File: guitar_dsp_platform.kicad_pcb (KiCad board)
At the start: 4 copper layers, 122 x 122 mm, 159 parts, among them J201 NMJ6HCD2, J202 NMJ6HCD2, J203 NMJ6HCD2, J204 NMJ6HCD2, J401 57PC5F, J402 57PC5F, J403 I2S, J501 PJ-002AH-SMT-TR, Q401 MMBT3904, Q501 SI2369DS-T1-BE3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

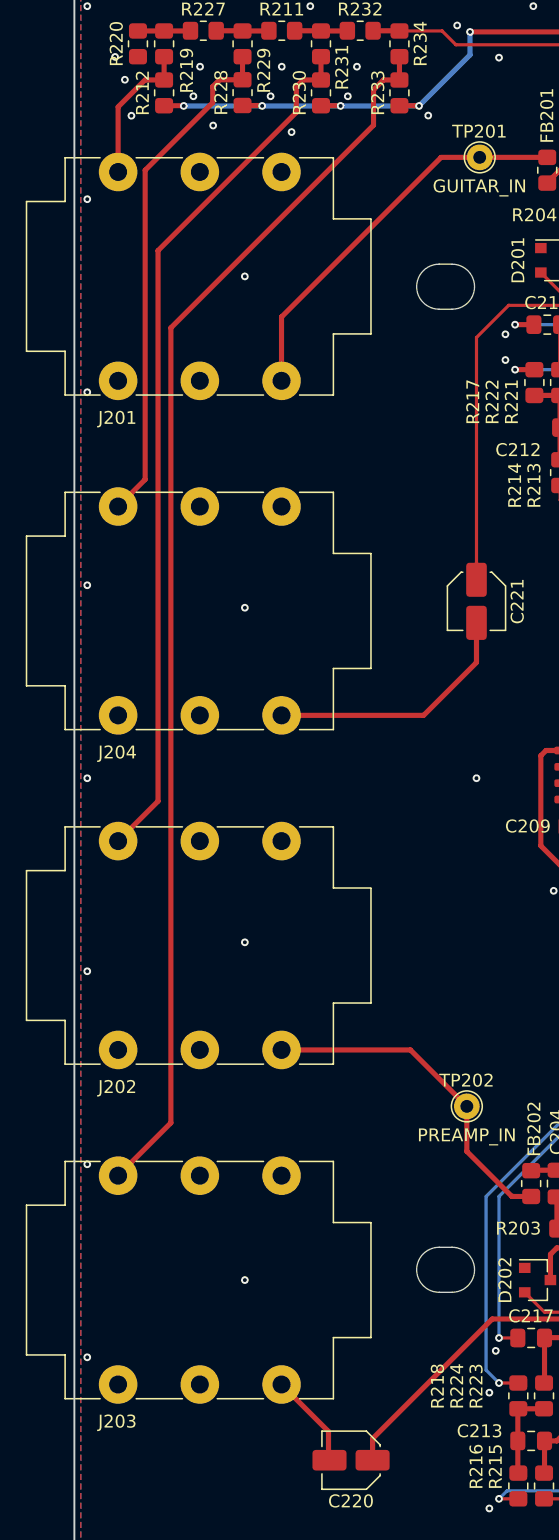
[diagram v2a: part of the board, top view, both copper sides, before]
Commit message: Adjust jack position after mechanical checks
Jacks will require two internal 1.2mm washers, and the external washer
supplied with the jacks.
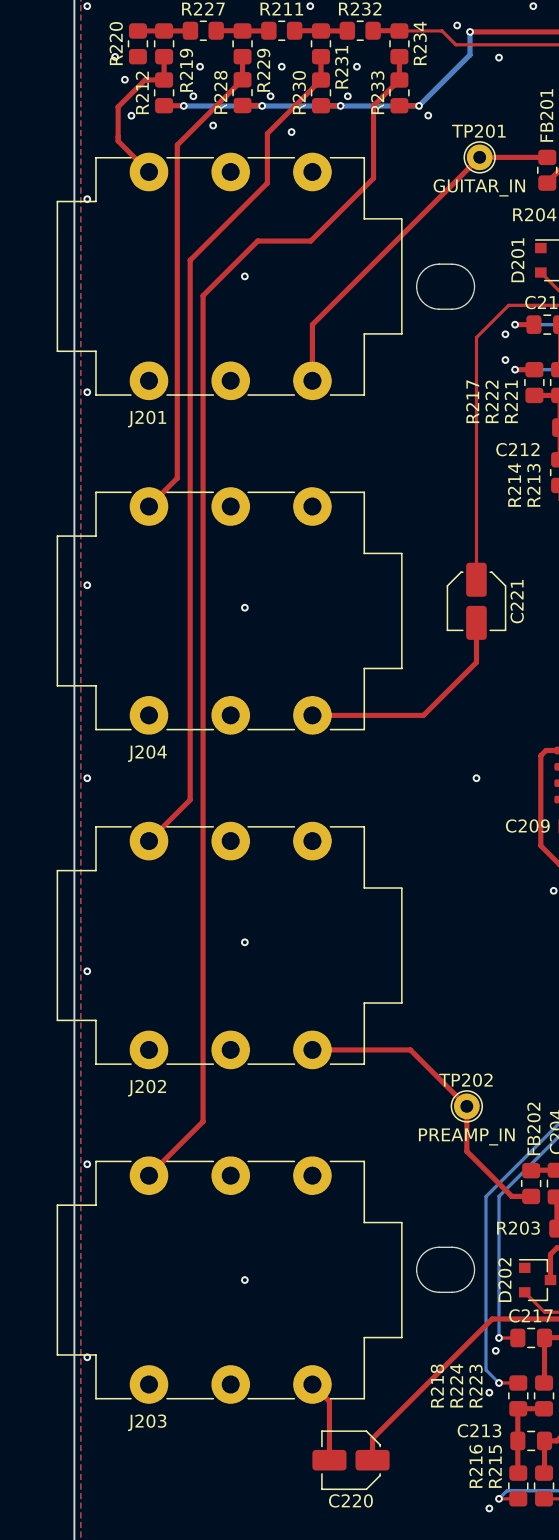
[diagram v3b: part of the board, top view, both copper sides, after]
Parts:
- moved J201 2.40 mm to (40.8, 61.0)
- moved J202 2.40 mm to (40.8, 113.0)
- moved J203 2.40 mm to (40.8, 139.0)
- moved J204 2.40 mm to (40.8, 87.0)
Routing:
- net Net-(FB201-Pad2): track 30.8 -> 28.0 mm
- net Net-(FB202-Pad2): track 26.2 -> 23.8 mm
- net Net-(C221-Pad2): track 19.9 -> 17.5 mm
- net /Analogue/PRE_O_DET_JACK: track 40.0 -> 38.0 mm
- net /Analogue/PRE_I_DET_JACK: track 68.3 -> 66.5 mm
- net Net-(C220-Pad2): track 7.43 -> 6.43 mm
- net /Analogue/G_DET_JACK: track 11.3 -> 12.3 mm
- net /Analogue/AMP_DET_JACK: track 96.7 -> 97.4 mm
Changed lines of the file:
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@@
   )
   (footprint "guitar_dsp_platform:Jack_6.35mm_Neutrik_NMJ6HCD2_Horizontal" locked (layer "F.Cu")
-    (at 38.35 61 180)
+    (at 40.75 61 180)
     (descr "M Series, 6.35mm (1/4in) stereo jack, switched, with chrome ferrule and straight PCB pins, https://www.neutrik.com/en/product/nmj6hcd2")
     (tags "neutrik jack m")
@@
   )
   (footprint "guitar_dsp_platform:Jack_6.35mm_Neutrik_NMJ6HCD2_Horizontal" locked (layer "F.Cu")
-    (at 38.35 87 180)
+    (at 40.75 87 180)
     (descr "M Series, 6.35mm (1/4in) stereo jack, switched, with chrome ferrule and straight PCB pins, https://www.neutrik.com/en/product/nmj6hcd2")
     (tags "neutrik jack m")
@@
   )
   (footprint "guitar_dsp_platform:Jack_6.35mm_Neutrik_NMJ6HCD2_Horizontal" locked (layer "F.Cu")
-    (at 38.35 139 180)
+    (at 40.75 139 180)
     (descr "M Series, 6.35mm (1/4in) stereo jack, switched, with chrome ferrule and straight PCB pins, https://www.neutrik.com/en/product/nmj6hcd2")
     (tags "neutrik jack m")
@@
   )
   (footprint "guitar_dsp_platform:Jack_6.35mm_Neutrik_NMJ6HCD2_Horizontal" locked (layer "F.Cu")
-    (at 38.35 113 180)
+    (at 40.75 113 180)
     (descr "M Series, 6.35mm (1/4in) stereo jack, switched, with chrome ferrule and straight PCB pins, https://www.neutrik.com/en/product/nmj6hcd2")
     (tags "neutrik jack m")
@@
   (segment (start 79.365 145.365) (end 79.365 143.475) (width 0.4) (layer "F.Cu") (net 40))
   (segment (start 79.9625 147) (end 77.5 147) (width 0.4) (layer "F.Cu") (net 40))
-  (segment (start 58.75 150.765) (end 58.75 151.75) (width 0.4) (layer "F.Cu") (net 41))
-  (segment (start 58.75 151.75) (end 58.75 152.925) (width 0.4) (layer "F.Cu") (net 41))
-  (segment (start 55.1 147.115) (end 58.75 150.765) (width 0.4) (layer "F.Cu") (net 41))
-  (segment (start 58.75 152.925) (end 58.825 153) (width 0.4) (layer "F.Cu") (net 41))
-  (segment (start 66.135 95.115) (end 55.1 95.115) (width 0.4) (layer "F.Cu") (net 42))
-  (segment (start 70.25 91) (end 66.135 95.115) (width 0.4) (layer "F.Cu") (net 42))
+  (segment (start 57.5 147.115) (end 58.825 148.44) (width 0.4) (layer "F.Cu") (net 41))
+  (segment (start 58.825 148.44) (end 58.825 153) (width 0.4) (layer "F.Cu") (net 41))
   (segment (start 70.25 87.925) (end 70.25 91) (width 0.4) (layer "F.Cu") (net 42))
+  (segment (start 66.135 95.115) (end 57.5 95.115) (width 0.4) (layer "F.Cu") (net 42))
+  (segment (start 70.25 91) (end 66.135 95.115) (width 0.4) (layer "F.Cu") (net 42))
   (segment (start 144.5375 132) (end 149 132) (width 1) (layer "F.Cu") (net 43))
   (segment (start 65.516 47.736) (end 64.262 47.736) (width 0.4) (layer "F.Cu") (net 44))
@@
   (segment (start 127.7875 125.4625) (end 127.7875 124.074) (width 0.4) (layer "F.Cu") (net 49))
   (segment (start 127.75 120) (end 127.75 122) (width 0.4) (layer "F.Cu") (net 49))
-  (segment (start 42.4 104.885) (end 45.5 101.785) (width 0.4) (layer "F.Cu") (net 50))
-  (segment (start 56.25 46.25) (end 56.764 45.736) (width 0.4) (layer "F.Cu") (net 50))
-  (segment (start 45.5 101.785) (end 45.5 59) (width 0.4) (layer "F.Cu") (net 50))
-  (segment (start 56.764 45.736) (end 58.166 45.736) (width 0.4) (layer "F.Cu") (net 50))
+  (segment (start 48 101.685) (end 48 59.75) (width 0.4) (layer "F.Cu") (net 50))
+  (segment (start 54 49.902) (end 58.166 45.736) (width 0.4) (layer "F.Cu") (net 50))
+  (segment (start 44.8 104.885) (end 48 101.685) (width 0.4) (layer "F.Cu") (net 50))
+  (segment (start 54 53.75) (end 54 49.902) (width 0.4) (layer "F.Cu") (net 50))
+  (segment (start 48 59.75) (end 54 53.75) (width 0.4) (layer "F.Cu") (net 50))
   (segment (start 58.166 43.926) (end 58.166 45.736) (width 0.4) (layer "F.Cu") (net 50))
-  (segment (start 56.25 48.25) (end 56.25 46.25) (width 0.4) (layer "F.Cu") (net 50))
-  (segment (start 45.5 59) (end 56.25 48.25) (width 0.4) (layer "F.Cu") (net 50))
+  (segment (start 42.4 50.15) (end 42.4 47.82937) (width 0.4) (layer "F.Cu") (net 51))
   (segment (start 44.49337 45.736) (end 45.974 45.736) (width 0.4) (layer "F.Cu") (net 51))
+  (segment (start 42.4 50.15) (end 42.4 50.485) (width 0.4) (layer "F.Cu") (net 51))
   (segment (start 42.4 47.82937) (end 44.49337 45.736) (width 0.4) (layer "F.Cu") (net 51))
   (segment (start 45.974 43.926) (end 45.974 45.736) (width 0.4) (layer "F.Cu") (net 51))
-  (segment (start 42.4 52.885) (end 42.4 47.82937) (width 0.4) (layer "F.Cu") (net 51))
+  (segment (start 42.4 50.485) (end 44.8 52.885) (width 0.4) (layer "F.Cu") (net 51))
   (segment (start 78.25 57.75) (end 79.25 57.75) (width 0.4) (layer "F.Cu") (net 52))
   (segment (start 79.25 57.75) (end 80.25 57.75) (width 0.4) (layer "F.Cu") (net 52))
@@
   (segment (start 77.25 59.75) (end 77.25 58.75) (width 0.4) (layer "F.Cu") (net 52))
   (segment (start 80.25 57.75) (end 80.65 58.15) (width 0.4) (layer "F.Cu") (net 52))
-  (segment (start 50.28 45.72) (end 49.75 46.25) (width 0.4) (layer "F.Cu") (net 53))
-  (segment (start 44.5 76.785) (end 42.4 78.885) (width 0.4) (layer "F.Cu") (net 53))
-  (segment (start 49.75 46.25) (end 49.75 47.5) (width 0.4) (layer "F.Cu") (net 53))
+  (segment (start 47 50.79) (end 47 76.685) (width 0.4) (layer "F.Cu") (net 53))
   (segment (start 52.07 43.926) (end 52.07 45.72) (width 0.4) (layer "F.Cu") (net 53))
-  (segment (start 52.07 45.72) (end 50.28 45.72) (width 0.4) (layer "F.Cu") (net 53))
-  (segment (start 49.75 47.5) (end 44.5 52.75) (width 0.4) (layer "F.Cu") (net 53))
-  (segment (start 44.5 52.75) (end 44.5 76.785) (width 0.4) (layer "F.Cu") (net 53))
+  (segment (start 52.07 45.72) (end 47 50.79) (width 0.4) (layer "F.Cu") (net 53))
+  (segment (start 47 76.685) (end 44.8 78.885) (width 0.4) (layer "F.Cu") (net 53))
   (segment (start 78.5 136) (end 78.5 135) (width 0.4) (layer "F.Cu") (net 54))
   (segment (start 76 137) (end 76.5 136.5) (width 0.4) (layer "F.Cu") (net 54))
@@
   (segment (start 141.25 117.55) (end 142.5 118.8) (width 0.25) (layer "F.Cu") (net 56))
   (segment (start 139.25 116.5) (end 140.3 117.55) (width 0.25) (layer "F.Cu") (net 56))
-  (segment (start 46.5 126.785) (end 46.5 65) (width 0.4) (layer "F.Cu") (net 57))
-  (segment (start 62.25 49.25) (end 62.25 46.5) (width 0.4) (layer "F.Cu") (net 57))
-  (segment (start 42.4 130.885) (end 46.5 126.785) (width 0.4) (layer "F.Cu") (net 57))
-  (segment (start 63.014 45.736) (end 64.262 45.736) (width 0.4) (layer "F.Cu") (net 57))
-  (segment (start 62.25 46.5) (end 63.014 45.736) (width 0.4) (layer "F.Cu") (net 57))
+  (segment (start 57.375 58.25) (end 62.25 53.375) (width 0.4) (layer "F.Cu") (net 57))
+  (segment (start 53.25 58.25) (end 57.375 58.25) (width 0.4) (layer "F.Cu") (net 57))
+  (segment (start 62.25 47.748) (end 64.262 45.736) (width 0.4) (layer "F.Cu") (net 57))
+  (segment (start 49 62.5) (end 53.25 58.25) (width 0.4) (layer "F.Cu") (net 57))
+  (segment (start 44.8 130.885) (end 49 126.685) (width 0.4) (layer "F.Cu") (net 57))
+  (segment (start 62.25 53.375) (end 62.25 47.748) (width 0.4) (layer "F.Cu") (net 57))
   (segment (start 64.262 43.926) (end 64.262 45.736) (width 0.4) (layer "F.Cu") (net 57))
-  (segment (start 46.5 65) (end 62.25 49.25) (width 0.4) (layer "F.Cu") (net 57))
+  (segment (start 49 126.685) (end 49 62.5) (width 0.4) (layer "F.Cu") (net 57))
   (segment (start 141.945 109.23) (end 138.52 109.23) (width 0.25) (layer "F.Cu") (net 58))
   (segment (start 139.25 118.5) (end 139.25 121.25) (width 0.25) (layer "F.Cu") (net 58))
@@
   (segment (start 93.5 98) (end 93.5 94.5) (width 0.25) (layer "F.Cu") (net 63))
   (segment (start 95.3765 98.75) (end 94.25 98.75) (width 0.25) (layer "F.Cu") (net 63))
-  (segment (start 67.5 51.75) (end 70.5 51.75) (width 0.4) (layer "F.Cu") (net 64))
+  (segment (start 57.5 64.75) (end 70.5 51.75) (width 0.4) (layer "F.Cu") (net 64))
   (segment (start 75.75 51.75) (end 70.5 51.75) (width 0.4) (layer "F.Cu") (net 64))
-  (segment (start 55.1 69.115) (end 55.1 64.15) (width 0.4) (layer "F.Cu") (net 64))
-  (segment (start 55.1 64.15) (end 67.5 51.75) (width 0.4) (layer "F.Cu") (net 64))
-  (segment (start 55.1 121.115) (end 65.115 121.115) (width 0.4) (layer "F.Cu") (net 65))
+  (segment (start 57.5 69.115) (end 57.5 64.75) (width 0.4) (layer "F.Cu") (net 64))
   (segment (start 65.115 121.115) (end 69.5 125.5) (width 0.4) (layer "F.Cu") (net 65))
+  (segment (start 57.5 121.115) (end 65.115 121.115) (width 0.4) (layer "F.Cu") (net 65))
   (segment (start 74.5 132.5) (end 73 132.5) (width 0.4) (layer "F.Cu") (net 65))
   (segment (start 69.5 129) (end 69.5 125.5) (width 0.4) (layer "F.Cu") (net 65))

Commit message: Resolve some issues
- Add missing MIDI connector pins to symbol
- Isolate low-ESR capacitors from 1117
- Fix DRC errors in footprints
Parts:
- removed C511: 100u, Capacitor_SMD:CP_Elec_6.3x7.7
- added C405: 100n, Capacitor_SMD:C_0805_2012Metric_Pad1.18x1.45mm_HandSolder, F.Cu at (158.0, 120.5)
- added NT301: Net-Tie_2, NetTie:NetTie-2_SMD_Pad0.5mm, F.Cu at (95.2, 108.0)
- added R415: 0, Resistor_SMD:R_0805_2012Metric_Pad1.20x1.40mm_HandSolder, F.Cu at (158.0, 116.8)
- added R511: 33, Resistor_SMD:R_0805_2012Metric_Pad1.20x1.40mm_HandSolder, F.Cu at (129.2, 121.8)
- moved C507 2.51 mm to (129.2, 123.8)
- moved C510 2.51 mm to (127.7, 130.9)
- moved R506 2.51 mm to (132.2, 122.8)
- moved R507 2.51 mm to (134.3, 122.8)
- moved R509 2.51 mm to (129.2, 119.8)
- moved U503 2.51 mm to (127.7, 127.4)
- moved TP503 1.52 mm to (124.8, 133.8)
- moved FB503 1.27 mm to (125.5, 121.8)
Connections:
- FB503 pad 1: /Power Supplies/+5V_F -> Net-(FB503-Pad1)
- J401 pad 6: (no net) -> Net-(C405-Pad1)
- J401 pad 7: (no net) -> Net-(C405-Pad1)
- J402 pad 6: (no net) -> Net-(J402-Pad6)
- J402 pad 7: (no net) -> Net-(J402-Pad6)
- R509 pad 2: /Power Supplies/+5V_F -> Net-(FB503-Pad1)
- U301 pad 28: GND -> /Audio Codec/MODE
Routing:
- net Net-(C405-Pad1): track 0.00 -> 14.0 mm
- net Net-(J402-Pad6): track 0.00 -> 14.0 mm
- net Net-(FB503-Pad1): track 0.00 -> 4.58 mm
- net +3V3: track 63.1 -> 65.7 mm
- net /Power Supplies/+5V_F: track 9.50 -> 7.50 mm
- net +5VA: track 219.3 -> 221.1 mm
- net /Audio Codec/MODE: track 0.00 -> 1.65 mm
- net Net-(FB402-Pad2): track 17.3 -> 16.0 mm
- net +5V: track 33.6 -> 32.7 mm
- net /Power Supplies/3V3_EN: track 12.5 -> 12.0 mm
- net GND: track 147.0 -> 146.7 mm, vias 226 -> 222
